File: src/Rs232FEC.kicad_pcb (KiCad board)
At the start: 2 copper layers, 24 x 27.9 mm, 24 parts, among them J1 B3B-XH-A, P1 105444-0001, Q1 DMP3099L-13, U1 FT232RL, U2 MAX232IDR

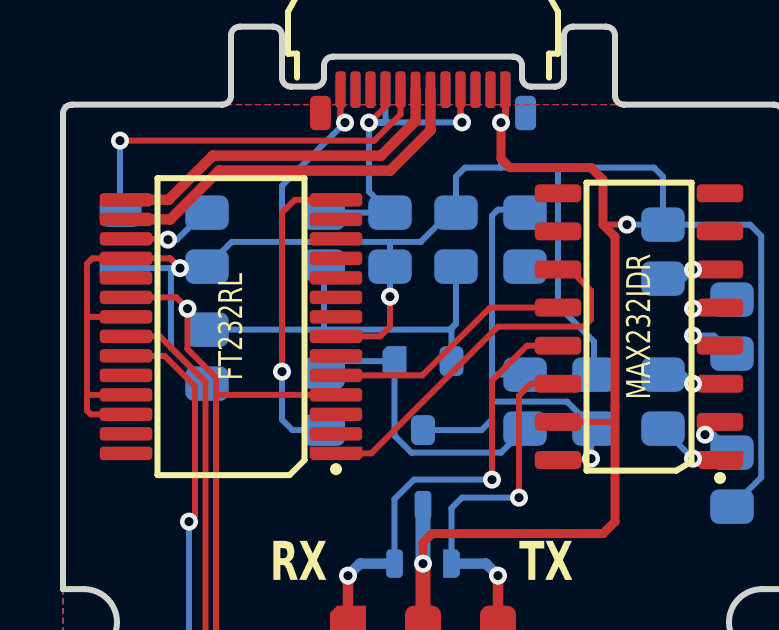
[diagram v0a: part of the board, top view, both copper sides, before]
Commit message: Added RTS/CTS loopback
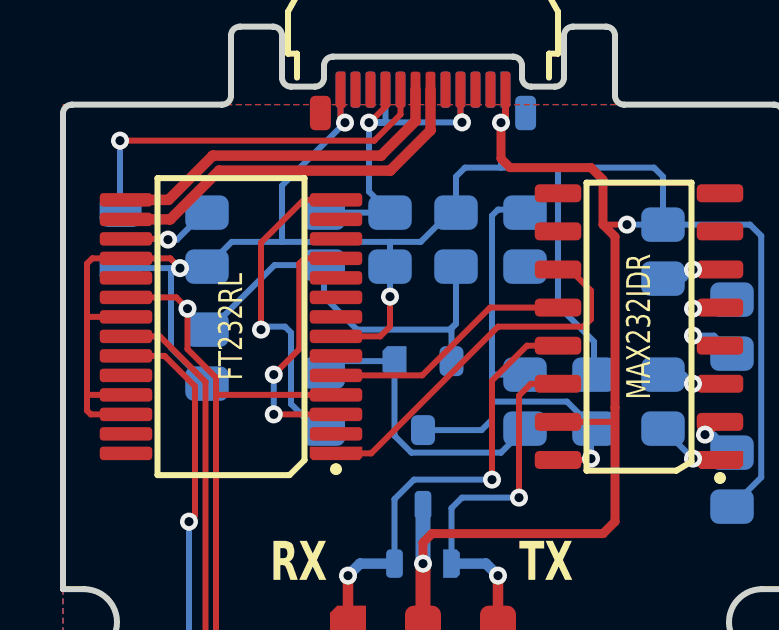
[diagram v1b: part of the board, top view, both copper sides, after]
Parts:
- renumbered C11 to C6
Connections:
- U1 pad 11: (no net) -> RTS_CTS
- U1 pad 3: (no net) -> RTS_CTS
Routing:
- net RTS_CTS: track 0.00 -> 8.75 mm, vias 0 -> 2
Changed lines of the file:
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@@
   (net 23 "VS-")
   (net 24 "VS+")
+  (net 25 "RTS_CTS")
   (footprint "Medo64:R (0805)" (layer "F.Cu")
     (at 40.4 44.1 180)
@@
       (thermal_bridge_angle 45))
     (pad "3" smd roundrect (at -3.5 -2.925 180) (size 1.75 0.45) (layers "F.Cu" "F.Paste" "F.Mask") (roundrect_rratio 0.25)
-      (thermal_bridge_angle 45))
+      (net 25 "RTS_CTS") (thermal_bridge_angle 45))
     (pad "4" smd roundrect (at -3.5 -2.275 180) (size 1.75 0.45) (layers "F.Cu" "F.Paste" "F.Mask") (roundrect_rratio 0.25)
       (net 3 "5V") (thermal_bridge_angle 45))
@@
       (thermal_bridge_angle 45))
     (pad "11" smd roundrect (at -3.5 2.275 180) (size 1.75 0.45) (layers "F.Cu" "F.Paste" "F.Mask") (roundrect_rratio 0.25)
-      (thermal_bridge_angle 45))
+      (net 25 "RTS_CTS") (thermal_bridge_angle 45))
     (pad "12" smd roundrect (at -3.5 2.925 180) (size 1.75 0.45) (layers "F.Cu" "F.Paste" "F.Mask") (roundrect_rratio 0.25)
       (thermal_bridge_angle 45))
@@
     (tags "CAPC2013X140N")
     (attr smd)
-    (fp_text reference "C11" (at 0 1.6 90) (layer "B.SilkS") hide
+    (fp_text reference "C6" (at 0 1.6 90) (layer "B.SilkS") hide
         (effects (font (size 0.8 0.6) (thickness 0.15) bold) (justify mirror))
     )
@@
   (via (at 24.15 29.4) (size 0.6) (drill 0.3) (layers "F.Cu" "B.Cu") (net 3))
   (via (at 25.099647 42.399647) (size 0.6) (drill 0.3) (layers "F.Cu" "B.Cu") (net 3))
+  (segment (start 33.1 29.9) (end 32.9 30.1) (width 0.2) (layer "B.Cu") (net 3))
+  (segment (start 32.9 30.1) (end 29.8 30.1) (width 0.2) (layer "B.Cu") (net 3))
   (segment (start 25.099647 42.399647) (end 25.1 42.4) (width 0.2) (layer "B.Cu") (net 3))
   (segment (start 24.8 30.1) (end 24.15 29.45) (width 0.2) (layer "B.Cu") (net 3))
   (segment (start 32.95 30.05) (end 33.1 29.9) (width 0.2) (layer "B.Cu") (net 3))
-  (segment (start 33.1 29.9) (end 32.9 30.1) (width 0.2) (layer "B.Cu") (net 3))
-  (segment (start 32.9 30.1) (end 28.7 30.1) (width 0.2) (layer "B.Cu") (net 3))
-  (segment (start 28.7 30.1) (end 28.7 27.95) (width 0.2) (layer "B.Cu") (net 3))
+  (segment (start 29.8 30.1) (end 28.7 29) (width 0.2) (layer "B.Cu") (net 3))
+  (segment (start 28.7 29) (end 28.7 27.95) (width 0.2) (layer "B.Cu") (net 3))
   (segment (start 24.15 29.45) (end 24.15 29.4) (width 0.2) (layer "B.Cu") (net 3))
   (segment (start 25.1 42.4) (end 37.899988 42.4) (width 0.2) (layer "B.Cu") (net 3))
   (segment (start 32.95 31.15) (end 32.95 30.05) (width 0.2) (layer "B.Cu") (net 3))
   (segment (start 33.1 28) (end 33.1 29.9) (width 0.2) (layer "B.Cu") (net 3))
-  (segment (start 24.8 30.1) (end 28.7 30.1) (width 0.2) (layer "B.Cu") (net 3))
+  (segment (start 27.05 27.95) (end 24.9 30.1) (width 0.2) (layer "B.Cu") (net 3))
+  (segment (start 27.05 27.95) (end 28.7 27.95) (width 0.2) (layer "B.Cu") (net 3))
   (segment (start 31.975 31.625) (end 34.235 29.365) (width 0.2) (layer "F.Cu") (net 4))
   (segment (start 34.235 29.365) (end 36.5 29.365) (width 0.2) (layer "F.Cu") (net 4))
@@
   (segment (start 31.05 31.15) (end 29.1 31.15) (width 0.2) (layer "B.Cu") (net 15))
   (segment (start 35.4 33.4) (end 34.6 34.2) (width 0.2) (layer "B.Cu") (net 15))
-  (segment (start 29.1 25.775) (end 27.725 25.775) (width 0.2) (layer "F.Cu") (net 16))
-  (segment (start 27.725 25.775) (end 27.3 26.2) (width 0.2) (layer "F.Cu") (net 16))
-  (segment (start 27.3 26.2) (end 27.3 31.5) (width 0.2) (layer "F.Cu") (net 16))
-  (via (at 27.3 31.5) (size 0.6) (drill 0.3) (layers "F.Cu" "B.Cu") (net 16))
-  (segment (start 28.9 33.45) (end 27.65 33.45) (width 0.2) (layer "B.Cu") (net 16))
-  (segment (start 27.65 33.45) (end 27.3 33.1) (width 0.2) (layer "B.Cu") (net 16))
-  (segment (start 27.3 33.1) (end 27.3 31.5) (width 0.2) (layer "B.Cu") (net 16))
+  (segment (start 29.1 25.775) (end 28.025 25.775) (width 0.2) (layer "F.Cu") (net 16))
+  (segment (start 28.025 25.775) (end 26.6 27.2) (width 0.2) (layer "F.Cu") (net 16))
+  (segment (start 26.6 27.2) (end 26.6 30) (width 0.2) (layer "F.Cu") (net 16))
+  (via (at 26.6 30.1) (size 0.6) (drill 0.3) (layers "F.Cu" "B.Cu") (net 16))
+  (segment (start 28.475 33.45) (end 27.6 32.575) (width 0.2) (layer "B.Cu") (net 16))
+  (segment (start 27.4 30) (end 26.6 30) (width 0.2) (layer "B.Cu") (net 16))
+  (segment (start 27.6 32.575) (end 27.6 30.2) (width 0.2) (layer "B.Cu") (net 16))
+  (segment (start 27.6 30.2) (end 27.4 30) (width 0.2) (layer "B.Cu") (net 16))
   (segment (start 41.9 31.905) (end 40.905 31.905) (width 0.2) (layer "F.Cu") (net 17))
   (via (at 41 31.905) (size 0.6) (drill 0.3) (layers "F.Cu" "B.Cu") (net 17))
@@
   (segment (start 41.7 33.6) (end 41.4 33.6) (width 0.2) (layer "B.Cu") (net 24))
   (segment (start 42.3 34.2) (end 41.7 33.6) (width 0.2) (layer "B.Cu") (net 24))
+  (segment (start 28.05 27.725) (end 27.875 27.9) (width 0.2) (layer "F.Cu") (net 25))
+  (segment (start 29.1 27.725) (end 28.05 27.725) (width 0.2) (layer "F.Cu") (net 25))
+  (segment (start 27.875 30.749994) (end 27.025 31.599994) (width 0.2) (layer "F.Cu") (net 25))
+  (segment (start 29.1 32.925) (end 27.025 32.925) (width 0.2) (layer "F.Cu") (net 25))
+  (segment (start 27.875 27.9) (end 27.875 30.749994) (width 0.2) (layer "F.Cu") (net 25))
+  (via (at 27.025 31.599994) (size 0.6) (drill 0.3) (layers "F.Cu" "B.Cu") (net 25))
+  (via (at 27.025 32.925) (size 0.6) (drill 0.3) (layers "F.Cu" "B.Cu") (net 25))
+  (segment (start 27.025 32.925) (end 27.025 31.599994) (width 0.2) (layer "B.Cu") (net 25))
   (zone (net 7) (net_name "GND") (layers "F&B.Cu") (hatch edge 0.5)
     (connect_pads (clearance 0.25))

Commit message: Changed protection diode
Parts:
- D1: value SM12T1G -> PESD12VL2BT
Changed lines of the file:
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@@
         (effects (font (size 0.8 0.6) (thickness 0.15)) (justify mirror))
     )
-    (fp_text value "SM12T1G" (at 0 -2.2) (layer "B.SilkS") hide
+    (fp_text value "PESD12VL2BT" (at 0 -2.2) (layer "B.SilkS") hide
         (effects (font (size 0.8 0.6) (thickness 0.15)) (justify mirror))
     )

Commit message: Minor refactorings
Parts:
- moved D1 2.88 mm to (32.0, 39.8)
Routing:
- net GND: track 111.2 -> 110.0 mm
- net RS232_TX: track 13.3 -> 14.3 mm
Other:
- board text added: "GND"

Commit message: Minor refactoring
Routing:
- net RS232_RX: track 16.0 -> 15.0 mm
- net RS232_TX: track 14.3 -> 13.3 mm
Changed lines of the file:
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@@
   (segment (start 25.1 32.3) (end 25.1 42.5) (width 0.2) (layer "F.Cu") (net 3))
   (segment (start 25.125 32.275) (end 25.1 32.3) (width 0.2) (layer "F.Cu") (net 3))
-  (segment (start 39.9 42.4) (end 37.899988 42.4) (width 0.2) (layer "F.Cu") (net 3))
   (segment (start 24.15 29.4) (end 24.15 30.75) (width 0.2) (layer "F.Cu") (net 3))
   (segment (start 24.65 42.849294) (end 24.65 44.1) (width 0.2) (layer "F.Cu") (net 3))
@@
   (segment (start 25.1 31.7) (end 25.1 32.3) (width 0.2) (layer "F.Cu") (net 3))
   (segment (start 25.1 42.4) (end 25.1 42.5) (width 0.2) (layer "F.Cu") (net 3))
-  (segment (start 41.35 43.85) (end 39.9 42.4) (width 0.2) (layer "F.Cu") (net 3))
   (segment (start 25.099647 42.399647) (end 24.65 42.849294) (width 0.2) (layer "F.Cu") (net 3))
+  (segment (start 41.35 43.85) (end 40.1 42.6) (width 0.2) (layer "F.Cu") (net 3))
+  (segment (start 40.1 42.6) (end 37.899988 42.6) (width 0.2) (layer "F.Cu") (net 3))
   (segment (start 29.1 32.275) (end 25.125 32.275) (width 0.2) (layer "F.Cu") (net 3))
   (segment (start 24.15 30.75) (end 25.1 31.7) (width 0.2) (layer "F.Cu") (net 3))
   (segment (start 22.1 29.025) (end 23.775 29.025) (width 0.2) (layer "F.Cu") (net 3))
   (segment (start 25.099647 42.399647) (end 25.1 42.4) (width 0.2) (layer "F.Cu") (net 3))
-  (via (at 37.899988 42.4) (size 0.6) (drill 0.3) (layers "F.Cu" "B.Cu") (net 3))
+  (via (at 37.899988 42.6) (size 0.6) (drill 0.3) (layers "F.Cu" "B.Cu") (net 3))
   (via (at 24.15 29.4) (size 0.6) (drill 0.3) (layers "F.Cu" "B.Cu") (net 3))
   (via (at 25.099647 42.399647) (size 0.6) (drill 0.3) (layers "F.Cu" "B.Cu") (net 3))
+  (segment (start 25.1 42.4) (end 37.699988 42.4) (width 0.2) (layer "B.Cu") (net 3))
   (segment (start 33.1 29.9) (end 32.9 30.1) (width 0.2) (layer "B.Cu") (net 3))
   (segment (start 32.9 30.1) (end 29.8 30.1) (width 0.2) (layer "B.Cu") (net 3))
-  (segment (start 25.099647 42.399647) (end 25.1 42.4) (width 0.2) (layer "B.Cu") (net 3))
   (segment (start 24.8 30.1) (end 24.15 29.45) (width 0.2) (layer "B.Cu") (net 3))
   (segment (start 32.95 30.05) (end 33.1 29.9) (width 0.2) (layer "B.Cu") (net 3))
+  (segment (start 37.699988 42.4) (end 37.899988 42.6) (width 0.2) (layer "B.Cu") (net 3))
   (segment (start 29.8 30.1) (end 28.7 29) (width 0.2) (layer "B.Cu") (net 3))
   (segment (start 28.7 29) (end 28.7 27.95) (width 0.2) (layer "B.Cu") (net 3))
   (segment (start 24.15 29.45) (end 24.15 29.4) (width 0.2) (layer "B.Cu") (net 3))
-  (segment (start 25.1 42.4) (end 37.899988 42.4) (width 0.2) (layer "B.Cu") (net 3))
   (segment (start 32.95 31.15) (end 32.95 30.05) (width 0.2) (layer "B.Cu") (net 3))
+  (segment (start 25.099647 42.399647) (end 25.1 42.4) (width 0.2) (layer "B.Cu") (net 3))
   (segment (start 33.1 28) (end 33.1 29.9) (width 0.2) (layer "B.Cu") (net 3))
   (segment (start 27.05 27.95) (end 24.9 30.1) (width 0.2) (layer "B.Cu") (net 3))
@@
   (via (at 42.3 46.5) (size 0.6) (drill 0.3) (layers "F.Cu" "B.Cu") (net 10))
   (via (at 24.2 36.5) (size 0.6) (drill 0.3) (layers "F.Cu" "B.Cu") (net 10))
-  (segment (start 24.2 40.55) (end 25.5 41.85) (width 0.2) (layer "B.Cu") (net 10))
-  (segment (start 38.5 42.222194) (end 38.5 46.1) (width 0.2) (layer "B.Cu") (net 10))
   (segment (start 38.9 46.5) (end 42.3 46.5) (width 0.2) (layer "B.Cu") (net 10))
   (segment (start 24.2 36.5) (end 24.2 40.55) (width 0.2) (layer "B.Cu") (net 10))
-  (segment (start 38.127806 41.85) (end 38.5 42.222194) (width 0.2) (layer "B.Cu") (net 10))
-  (segment (start 25.5 41.85) (end 38.127806 41.85) (width 0.2) (layer "B.Cu") (net 10))
+  (segment (start 38.5 42.4) (end 38.5 46.1) (width 0.2) (layer "B.Cu") (net 10))
+  (segment (start 24.2 40.55) (end 25.7 42.05) (width 0.2) (layer "B.Cu") (net 10))
   (segment (start 38.5 46.1) (end 38.9 46.5) (width 0.2) (layer "B.Cu") (net 10))
+  (segment (start 25.7 42.05) (end 38.15 42.05) (width 0.2) (layer "B.Cu") (net 10))
+  (segment (start 38.15 42.05) (end 38.5 42.4) (width 0.2) (layer "B.Cu") (net 10))
   (segment (start 39.45 44.1) (end 39.45 46.45) (width 0.2) (layer "F.Cu") (net 11))
   (segment (start 22.7 46.5) (end 22.7 44.15) (width 0.2) (layer "F.Cu") (net 12))
@@
   (segment (start 36.5 31.905) (end 35.645 31.905) (width 0.2) (layer "F.Cu") (net 21))
   (segment (start 35.645 31.905) (end 34.4 33.15) (width 0.2) (layer "F.Cu") (net 21))
-  (via (at 34.5 39.8) (size 0.6) (drill 0.3) (layers "F.Cu" "B.Cu") (net 21))
+  (via (at 34.5 40.8) (size 0.6) (drill 0.3) (layers "F.Cu" "B.Cu") (net 21))
   (via (at 34.4 36.65) (size 0.6) (drill 0.3) (layers "F.Cu" "B.Cu") (net 21))
+  (segment (start 34.5 40.8) (end 34.475002 40.775002) (width 0.35) (layer "B.Cu") (net 21))
   (segment (start 33 36.65) (end 32.55 37.1) (width 0.2) (layer "B.Cu") (net 21))
+  (segment (start 34.475002 40.775002) (end 32.95 40.775002) (width 0.35) (layer "B.Cu") (net 21))
   (segment (start 32.55 37.1) (end 32.55 40.15) (width 0.2) (layer "B.Cu") (net 21))
   (segment (start 34.4 36.65) (end 33 36.65) (width 0.2) (layer "B.Cu") (net 21))
-  (segment (start 34.5 39.8) (end 34.5 40.775002) (width 0.35) (layer "B.Cu") (net 21))
   (segment (start 32.55 40.15) (end 32.95 40.55) (width 0.2) (layer "B.Cu") (net 21))
-  (segment (start 34.5 40.775002) (end 32.95 40.775002) (width 0.35) (layer "B.Cu") (net 21))
   (segment (start 33.2 32.8) (end 33.2 35.35) (width 0.2) (layer "F.Cu") (net 22))
   (segment (start 35.365 30.635) (end 33.2 32.8) (width 0.2) (layer "F.Cu") (net 22))
   (segment (start 36.5 30.635) (end 35.365 30.635) (width 0.2) (layer "F.Cu") (net 22))
   (via (at 33.2 35.35) (size 0.6) (drill 0.3) (layers "F.Cu" "B.Cu") (net 22))
-  (via (at 29.5 39.8) (size 0.6) (drill 0.3) (layers "F.Cu" "B.Cu") (net 22))
+  (via (at 29.5 40.8) (size 0.6) (drill 0.3) (layers "F.Cu" "B.Cu") (net 22))
   (segment (start 33.2 35.35) (end 32.15 35.35) (width 0.2) (layer "B.Cu") (net 22))
   (segment (start 31.45 40.15) (end 31.05 40.55) (width 0.2) (layer "B.Cu") (net 22))
-  (segment (start 29.5 40.775002) (end 31.05 40.775002) (width 0.35) (layer "B.Cu") (net 22))
   (segment (start 31.45 36.05) (end 31.45 40.15) (width 0.2) (layer "B.Cu") (net 22))
   (segment (start 32.15 35.35) (end 31.45 36.05) (width 0.2) (layer "B.Cu") (net 22))
-  (segment (start 29.5 39.8) (end 29.5 40.775002) (width 0.35) (layer "B.Cu") (net 22))
+  (segment (start 29.5 40.8) (end 29.524998 40.775002) (width 0.35) (layer "B.Cu") (net 22))
+  (segment (start 29.524998 40.775002) (end 31.05 40.775002) (width 0.35) (layer "B.Cu") (net 22))
   (segment (start 41.9 28.095) (end 41.005 28.095) (width 0.2) (layer "F.Cu") (net 23))
   (segment (start 41.005 28.095) (end 41 28.1) (width 0.2) (layer "F.Cu") (net 23))

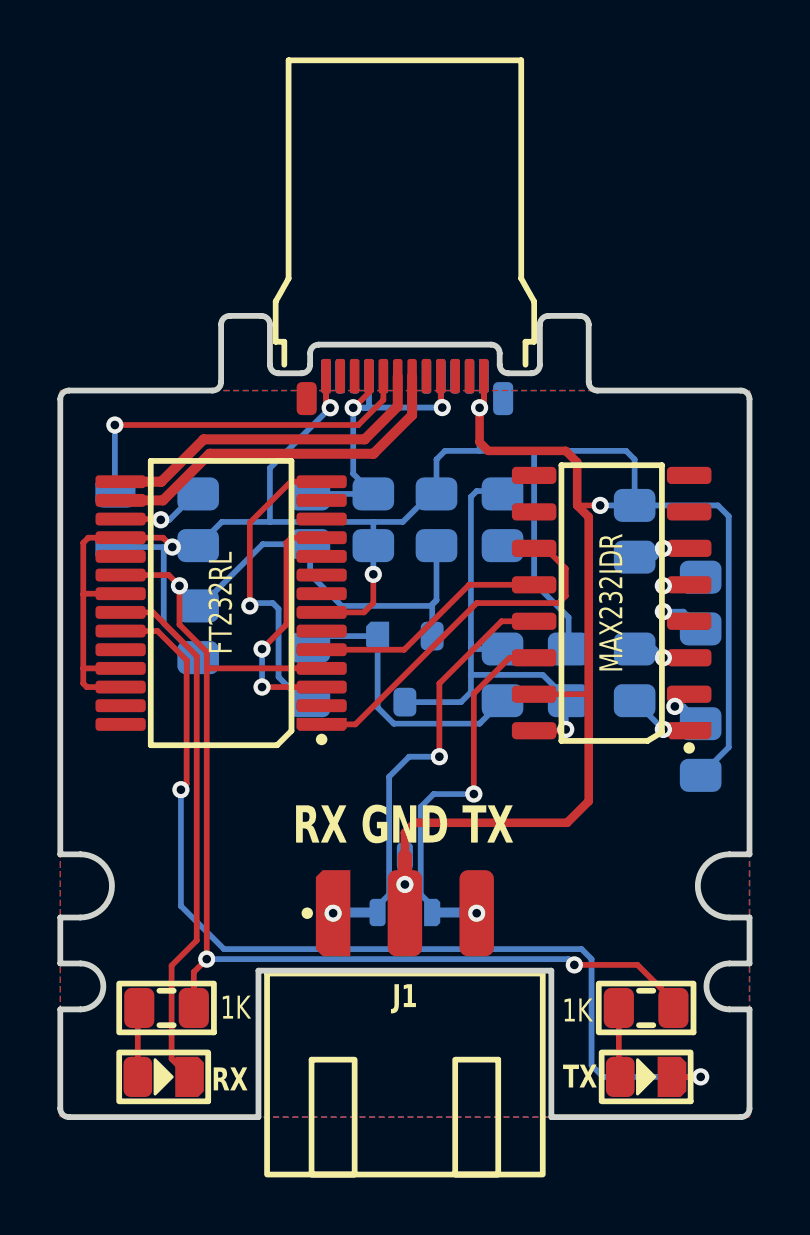
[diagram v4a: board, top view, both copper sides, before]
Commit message: Moved LEDs to bottom
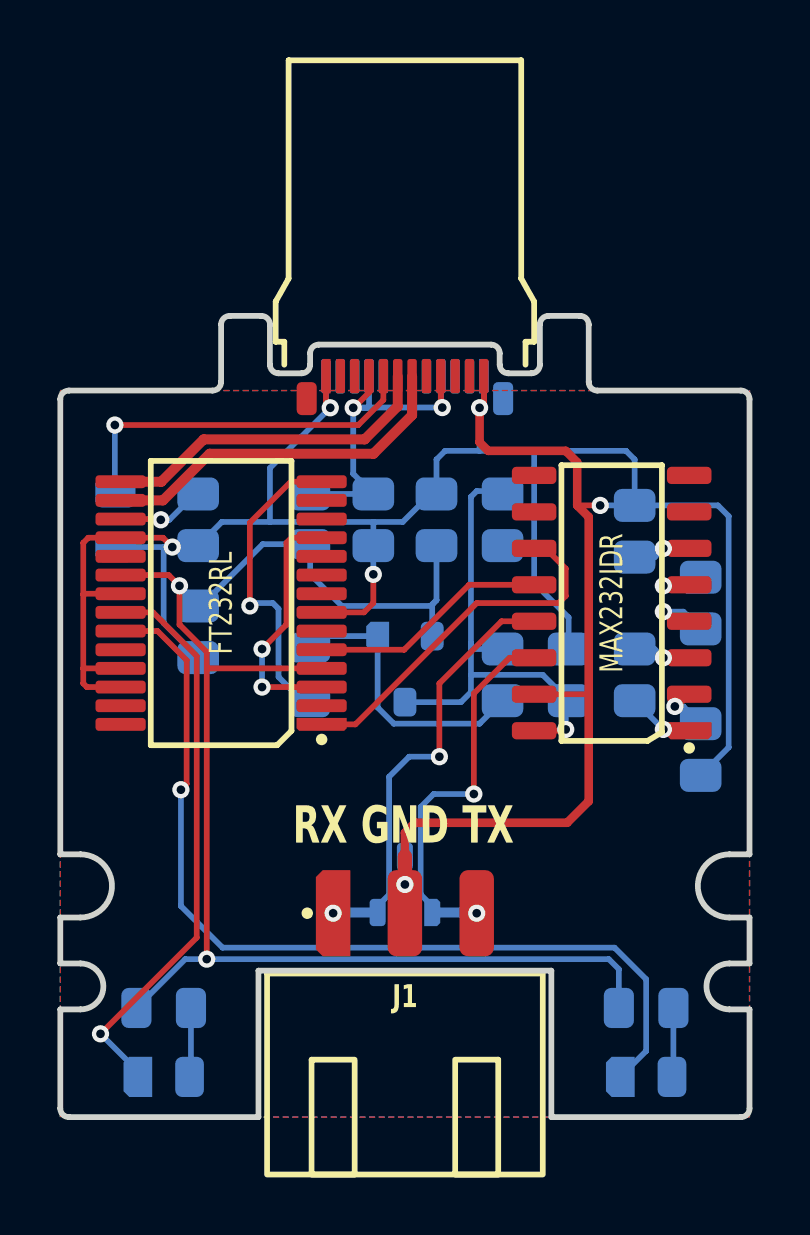
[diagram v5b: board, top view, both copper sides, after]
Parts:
- DS1, DS2, R1, R2: moved to B.Cu
- moved R1 0.10 mm to (23.6, 44.1), turned to 0 degrees
- turned DS1 to 0 degrees
- turned DS2 to 0 degrees
- turned R2 to 0 degrees
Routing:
- net LED_TXD: track 35.1 -> 32.4 mm, vias 2 -> 1
- net LED_RXD: track 18.6 -> 19.7 mm, vias 0 -> 1
- net 5V: track 53.4 -> 53.7 mm, vias 3 -> 2

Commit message: Added PWREN pullup and moved LED 5V to switched
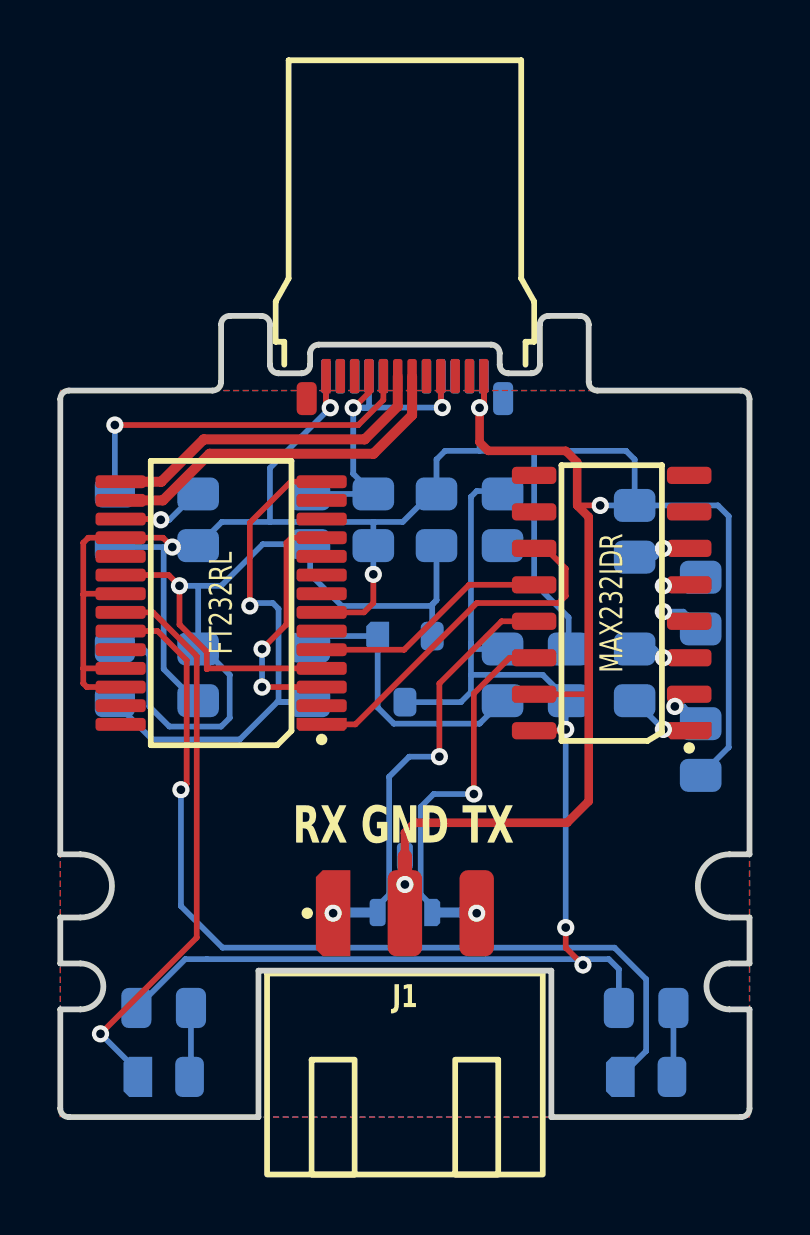
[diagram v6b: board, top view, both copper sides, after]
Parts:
- added R5: 10K, Medo64:R (0805), B.Cu at (21.9, 32.5)
- moved C2 1.50 mm to (24.8, 32.5)
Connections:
- R1 pad 1: 5V -> 5V_SW
- R2 pad 1: 5V -> 5V_SW
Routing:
- net 5V_SW: track 17.4 -> 45.5 mm, vias 1 -> 3
- net 5V: track 53.7 -> 35.2 mm, vias 2 -> 1
- net PWREN#: track 10.6 -> 19.0 mm
- net GND: track 110.0 -> 111.5 mm
